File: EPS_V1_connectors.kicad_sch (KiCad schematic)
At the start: 13 parts, among them J1 Conn_01x20_Socket, J2 Conn_01x30_Socket, J3 Conn_01x15_Socket, J4 Conn_01x04_Socket, SW1 OMRON D2F-L3-D (RIGHT), SW2 OMRON D2F-L3-D (LEFT), SW3 OMRON D2F-L3-D (RIGHT)

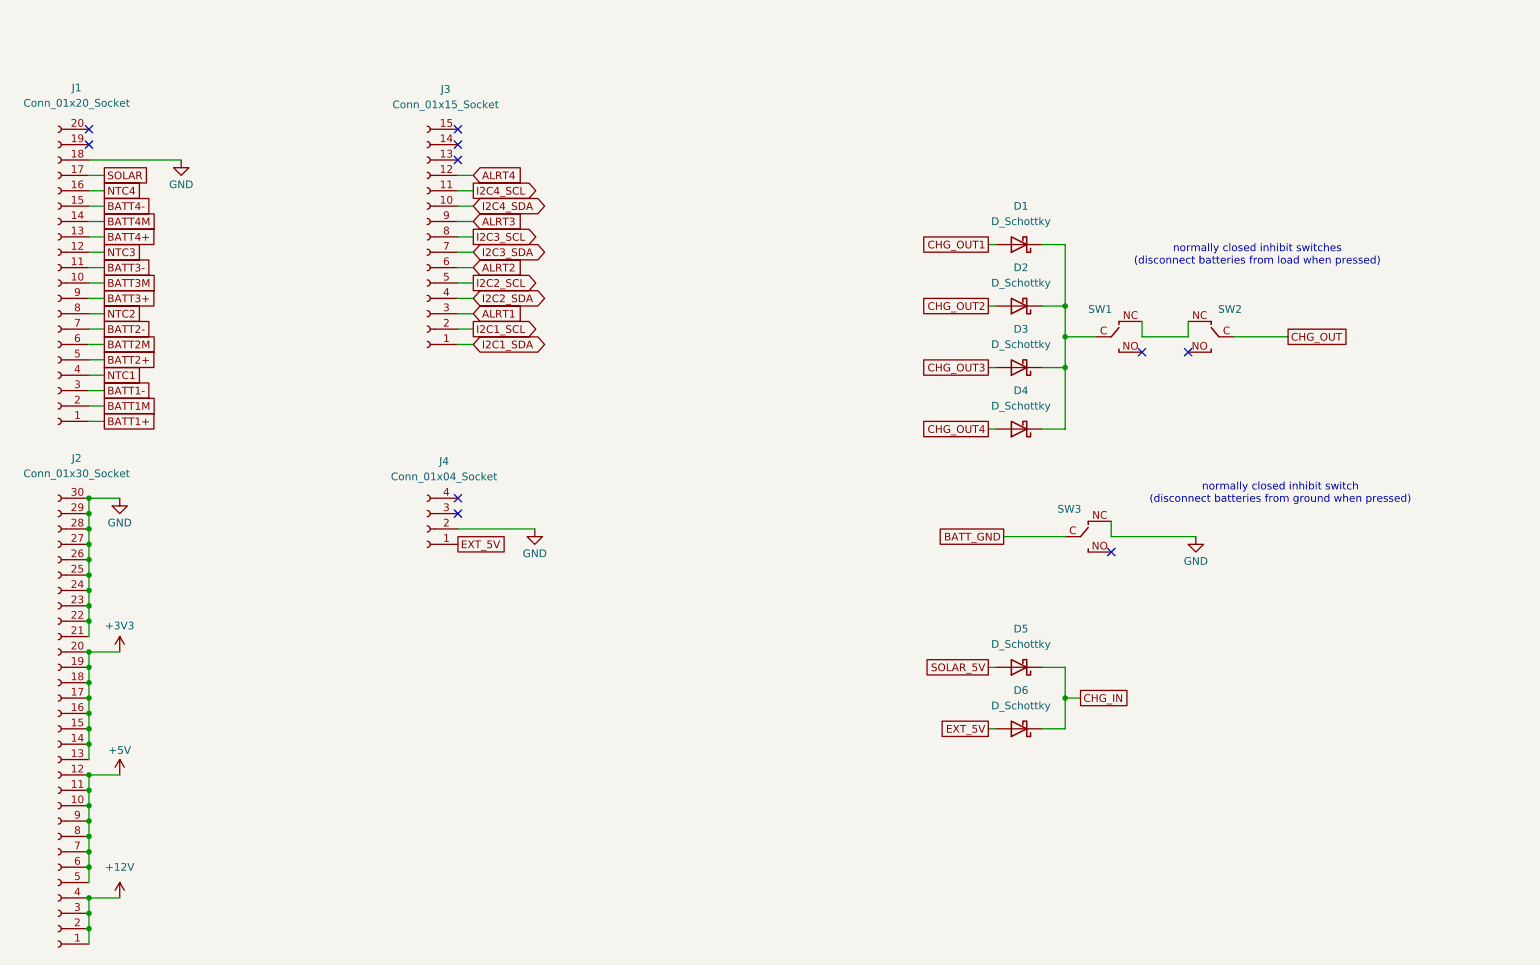
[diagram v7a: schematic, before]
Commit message: Add all footprints except connectors & switches, change to net ties over 0 ohm resistors
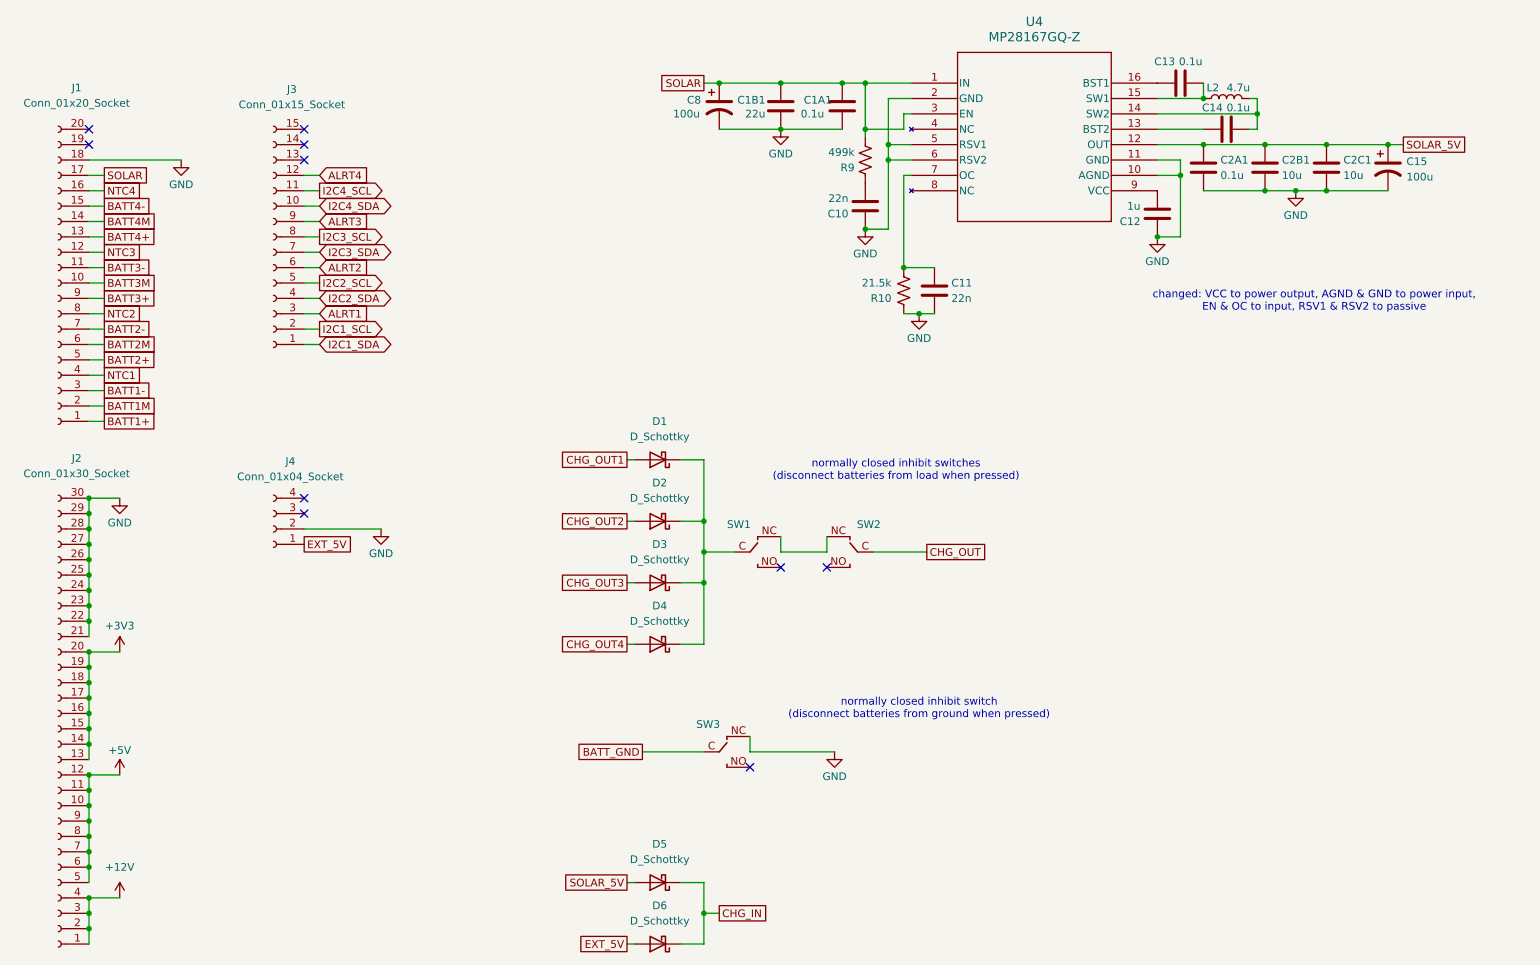
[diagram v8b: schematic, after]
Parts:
- added C10, C11: 22n, Capacitor_SMD:C_0603_1608Metric, symbol Device:C
- added C12: 1u, Capacitor_SMD:C_0603_1608Metric, symbol Device:C
- added C13, C14, C1A1, C2A1: 0.1u, Capacitor_SMD:C_0603_1608Metric, symbol Device:C
- added C15, C8: 100u, Capacitor_SMD:CP_Elec_6.3x5.4, symbol Device:C_Polarized_US
- added C1B1: 22u, Capacitor_SMD:C_0805_2012Metric, symbol Device:C
- added C2B1, C2C1: 10u, Capacitor_SMD:C_0805_2012Metric, symbol Device:C
- added L2: 4.7u, ASPI_7318_4R7M_T:IND_ASPI-7318-4R7M-T, symbol Device:L
- added R10: 21.5k, Resistor_SMD:R_0603_1608Metric, symbol Device:R_US
- added R9: 499k, Resistor_SMD:R_0603_1608Metric, symbol Device:R_US
- added U4: MP28167GQ-Z, MP28167GQ-Z:QFN-16_MP28167GQ_MNP, symbol MP28167GQ-Z:MP28167GQ-Z
- D1, D2, D3, D4, D5, D6: footprint (none) -> Diode_SMD:D_SOD-128; MPN (none) -> RSX301LAM30TR
- SW1, SW3: value OMRON D2F-L3-D (RIGHT) -> SWITCH
- SW2: value OMRON D2F-L3-D (LEFT) -> SWITCH
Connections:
- net GND: now also C10.1, C11.2, C12.1, C15.2, C1A1.2, C1B1.1, C2A1.2, C2B1.2, C2C1.2, C8.2, R10.1, U4.10 (AGND), U4.11 (GND), U4.2 (GND), U4.5 (RSV1), U4.6 (RSV2)
- net SOLAR: now also C1A1.1, C1B1.2, C8.1, R9.2, U4.1 (IN), U4.3 (EN)
- net SOLAR_5V: now also C15.1, C2A1.1, C2B1.1, C2C1.1, U4.12 (OUT)
- net +12V: no longer names the net of J2.1 (Pin_1), J2.2 (Pin_2), J2.3 (Pin_3), J2.4 (Pin_4)
- net +3V3: no longer names the net of J2.13 (Pin_13), J2.14 (Pin_14), J2.15 (Pin_15), J2.16 (Pin_16), J2.17 (Pin_17), J2.18 (Pin_18), J2.19 (Pin_19), J2.20 (Pin_20)
- net +5V: no longer names the net of J2.10 (Pin_10), J2.11 (Pin_11), J2.12 (Pin_12), J2.5 (Pin_5), J2.6 (Pin_6), J2.7 (Pin_7), J2.8 (Pin_8), J2.9 (Pin_9)
- new net: C10.2, R9.1
- new net: C11.1, R10.2, U4.7 (OC)
- new net: C13.2, L2.1, U4.15 (SW1)
- new net: C14.2, L2.2, U4.14 (SW2)
- new net: C14.1, U4.13 (BST2)
- new net: C13.1, U4.16 (BST1)
- new net: C12.2, U4.9 (VCC)
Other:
- note added: "changed: VCC to power output, AGND & GND to power input, EN & OC to input, RSV1 & RSV2 to passive"
- moved on the sheet: D1, D2, D3, D4, D5, D6, J3, J4, SW1, SW2, SW3
